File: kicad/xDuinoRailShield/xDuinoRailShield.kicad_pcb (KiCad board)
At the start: 2 copper layers, 36 parts, among them J5 Screw_Terminal_01x02, Q2 S8050, Q3 S8550, Q4 S8050, Q5 S8550, U1 TPS5430DDA, U2 6N137, U3 EL817

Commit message: Heavy refactoring
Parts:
- removed D2: D, Diode_SMD:D_SMA
- added D9: SS54, Diode_SMD:D_SMA, F.Cu at (153.9, 69.5)
- D4: value D_Schottky -> SS54; footprint Diode_SMD:D_SMC -> Diode_SMD:D_SMA
- D6, D7, D8: value D -> SS54
- R7: value 22 -> 20

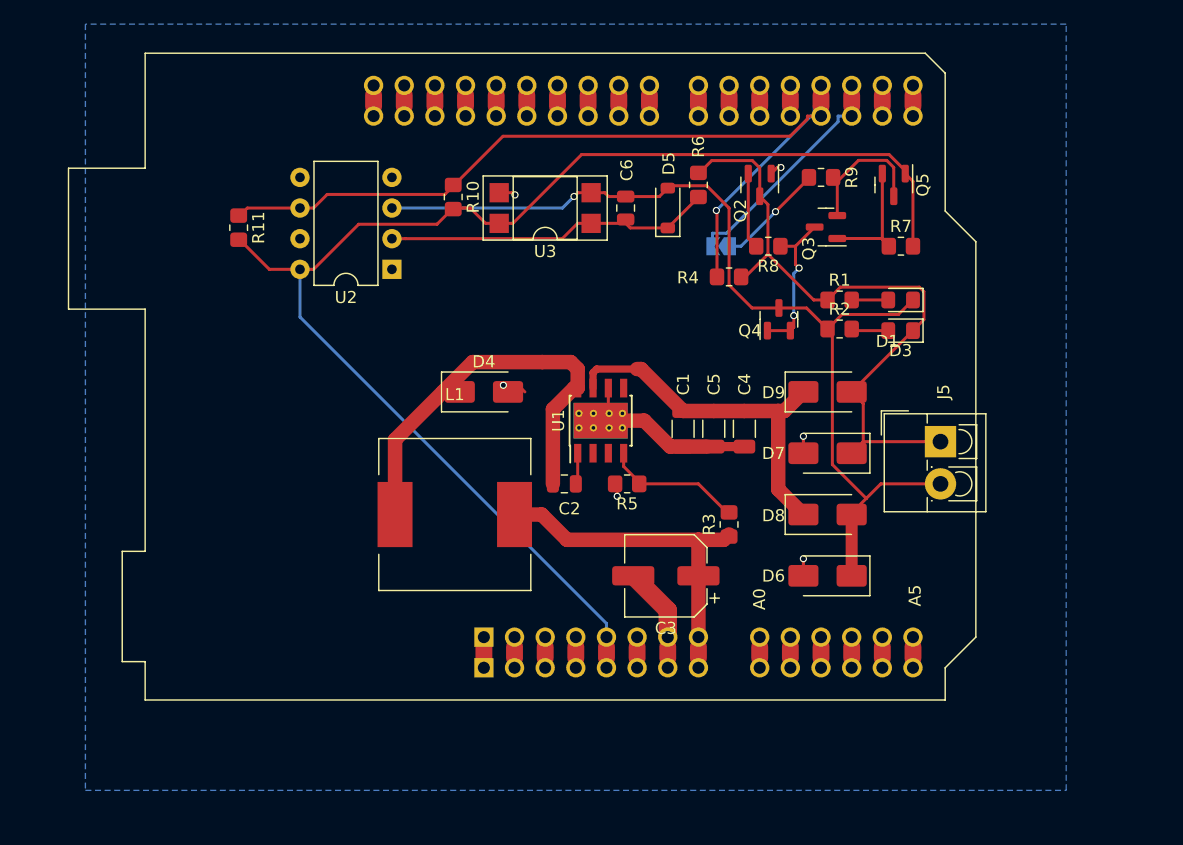
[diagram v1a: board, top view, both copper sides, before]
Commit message: More options, more Partnumbers
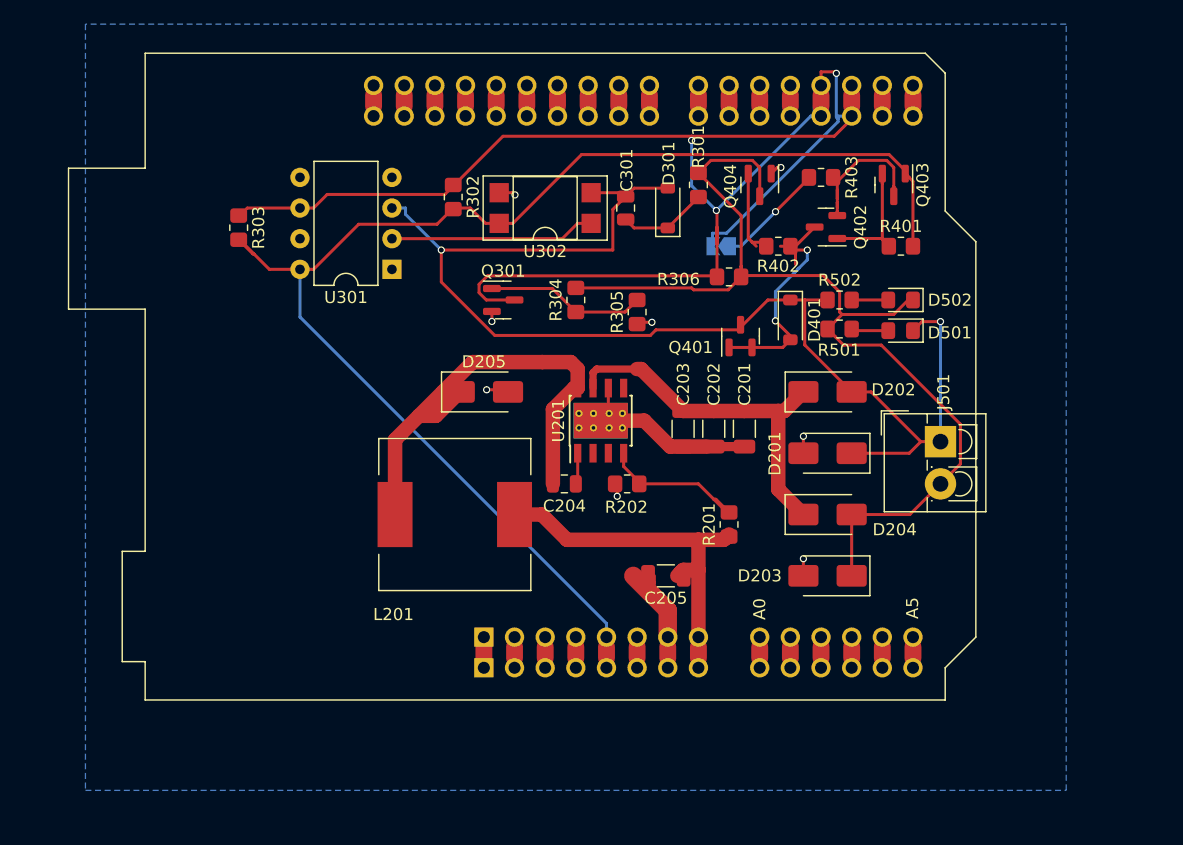
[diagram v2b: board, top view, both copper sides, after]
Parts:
- added D401: 1N4148W, Diode_SMD:D_SOD-123, F.Cu at (150.8, 63.5)
- added Q301: T2N7002BK, Package_TO_SOT_SMD:SOT-23, F.Cu at (127.0, 61.9)
- added R304: 6k8, Resistor_SMD:R_0805_2012Metric_Pad1.20x1.40mm_HandSolder, F.Cu at (133.0, 61.9)
- added R305: 6k8, Resistor_SMD:R_0805_2012Metric_Pad1.20x1.40mm_HandSolder, F.Cu at (138.1, 62.9)
- C205: renamed from C3; footprint Capacitor_SMD:CP_Elec_6.3x3.9 -> Capacitor_SMD:C_1206_3216Metric
- moved Q401 3.47 mm to (146.7, 64.9)
- moved R402 0.83 mm to (149.8, 57.4)
- renumbered A1 to A501, C4 to C201, C5 to C202, C1 to C203, C2 to C204, C6 to C301, D7 to D201, D9 to D202, D6 to D203, D8 to D204, D4 to D205, D5 to D301, D3 to D501, D1 to D502, J5 to J501, JP_RAILCOM1 to JP_RAILCOM401, L1 to L201, Q4 to Q401, Q3 to Q402, Q5 to Q403, Q2 to Q404, R3 to R201, R5 to R202, R6 to R301, R10 to R302, R11 to R303, R4 to R306, R7 to R401, R8 to R402, R9 to R403, R2 to R501, R1 to R502, U1 to U201, U2 to U301, U3 to U302
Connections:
- net Net-(D8-K) renamed DCC_VIN
- A501 pad 17: RAILCOM_DATA -> DCC_MM
- A501 pad 18: DCC_MM -> RAILCOM_DATA
- C301 pad 1: Net-(D5-K) -> Net-(D301-K)
- C301 pad 2: DCC_1 -> /DCC1
- D201 pad 1: DCC_0 -> /DCC1
- D202 pad 2: DCC_0 -> /DCC1
- D203 pad 1: DCC_1 -> /DCC0
- D204 pad 2: DCC_1 -> /DCC0
- D301 pad 1: Net-(D5-K) -> Net-(D301-K)
- D301 pad 2: DCC_1 -> /DCC1
- D501 pad 1: DCC_0 -> /DCC1
- D502 pad 1: DCC_1 -> /DCC0
- J501 pad 1: DCC_0 -> /DCC1
- J501 pad 2: DCC_1 -> /DCC0
- Q401 pad 3: DCC_1 -> /DCC1
- Q404 pad 3: DCC_0 -> /DCC0
- R301 pad 1: DCC_0 -> /DCC0
- R301 pad 2: Net-(D5-K) -> Net-(D301-K)
- R306 pad 1: DCC_0 -> /DCC0
- R501 pad 1: DCC_1 -> /DCC0
- R502 pad 1: DCC_0 -> /DCC1
- U301 pad 2: Net-(D5-K) -> DCC_0_1K3
- U301 pad 3: DCC_1 -> /DCC1
- U302 pad 1: Net-(D5-K) -> DCC_0_1K3
- U302 pad 2: DCC_1 -> /DCC1
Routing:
- net /DCC1: track 0.00 -> 106.7 mm, vias 0 -> 2
- net /DCC0: track 0.00 -> 87.5 mm
- net DCC_1: track 82.8 -> 0.00 mm, vias 1 -> 0
- net DCC_0: track 54.4 -> 0.00 mm
- net DCC_MM: track 72.1 -> 109.8 mm, vias 1 -> 2
- net Net-(D5-K): track 27.6 -> 0.00 mm
- net DCC_0_1K3: track 0.00 -> 17.0 mm
- net Net-(Q301-G): track 0.00 -> 13.3 mm
- net RAILCOM_DATA: track 19.4 -> 28.8 mm, vias 0 -> 1
- net Net-(D401-A): track 12.8 -> 20.7 mm
- net Net-(D301-K): track 0.00 -> 7.41 mm
- net GND: track 32.0 -> 36.9 mm, vias 6 -> 8
- net Net-(D205-K): track 34.8 -> 39.0 mm
- net VCC: track 29.4 -> 32.0 mm
- net +5V: track 111.9 -> 114.2 mm
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
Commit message: Leiterbahnbreiten anpassen
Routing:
- net GND: track 36.9 -> 63.5 mm, vias 8 -> 13
- net DCC_MM: track 109.8 -> 118.0 mm
- net RAILCOM_DATA: track 28.8 -> 21.5 mm, vias 1 -> 0
- net /DCC0: track 87.5 -> 84.9 mm
- net +5V: track 114.2 -> 116.6 mm
- net /DCC1: track 106.7 -> 105.4 mm, vias 2 -> 1
- net Net-(Q402-E): track 10.8 -> 9.97 mm

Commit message: Edge cuts
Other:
- board outline added: 68.6 x 53.3 mm
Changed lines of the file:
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@@
       ))
   )
+  (gr_line (start 163.503242 43.117028) (end 161.96181 41.575596)
+    (stroke (width 0.15) (type default)) (layer "Edge.Cuts"))
+  (gr_line (start 166.04 89.84) (end 166.04 56.82)
+    (stroke (width 0.15) (type default)) (layer "Edge.Cuts"))
+  (gr_line (start 161.96181 41.575596) (end 97.46 41.58)
+    (stroke (width 0.15) (type default)) (layer "Edge.Cuts"))
+  (gr_line (start 163.5 92.38) (end 166.04 89.84)
+    (stroke (width 0.15) (type default)) (layer "Edge.Cuts"))
+  (gr_line (start 163.5 54.28) (end 163.503242 43.117028)
+    (stroke (width 0.15) (type default)) (layer "Edge.Cuts"))
+  (gr_line (start 97.46 41.58) (end 97.46 94.92)
+    (stroke (width 0.15) (type default)) (layer "Edge.Cuts"))
+  (gr_line (start 163.5 94.92) (end 163.5 92.38)
+    (stroke (width 0.15) (type default)) (layer "Edge.Cuts"))
+  (gr_line (start 166.04 56.82) (end 163.5 54.28)
+    (stroke (width 0.15) (type default)) (layer "Edge.Cuts"))
+  (gr_line (start 97.46 94.92) (end 163.5 94.92)
+    (stroke (width 0.15) (type default)) (layer "Edge.Cuts"))
   (gr_text "ICSP" (at 161.492899 64.565 -90) (layer "Dwgs.User")
     (effects (font (size 1 1) (thickness 0.15)))
@@
     (polygon
       (pts
-        (xy 87.3 39.04)
-        (xy 87.3 102.54)
-        (xy 173.66 102.54)
+        (xy 89.84 39.04)
+        (xy 89.84 97.46)
+        (xy 173.66 97.46)
         (xy 173.66 39.04)
       )

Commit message: Another iteration on the layout
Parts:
- J501: footprint TerminalBlock_4Ucon:TerminalBlock_4Ucon_1x02_P3.50mm_Vertical -> TerminalBlock:TerminalBlock_bornier-2_P5.08mm
- U302: footprint Package_DIP:DIP-4_W7.62mm_SMDSocket_SmallPads -> Package_DIP:DIP-4_W8.89mm_SMDSocket_LongPads
- moved C301 2.98 mm to (139.7, 52.7), turned to 180 degrees
- moved C205 2.61 mm to (138.1, 83.7), turned to -90 degrees
- moved D301 2.54 mm to (140.6, 56.8)
- moved R201 2.54 mm to (143.2, 80.5)
- moved Q301 2.21 mm to (128.5, 60.3), turned to 180 degrees
- moved R302 1.38 mm to (121.8, 52.4)
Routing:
- net VCC: track 32.0 -> 26.7 mm
- net DCC_MM: track 118.0 -> 113.1 mm
- net Net-(U201-VSENSE): track 13.4 -> 9.06 mm
- net Net-(Q301-G): track 13.3 -> 9.72 mm
- net Net-(D401-A): track 20.7 -> 18.0 mm
- net unconnected-(A501-SDA/A4-Pad31): track 2.54 -> 0.00 mm
- net unconnected-(A501-SCL/A5-Pad32)_0: track 2.54 -> 0.00 mm
- net unconnected-(A501-D9-Pad24)_0: track 2.54 -> 0.00 mm
- net unconnected-(A501-D8-Pad23)_0: track 2.54 -> 0.00 mm
- net unconnected-(A501-D7-Pad22): track 2.54 -> 0.00 mm
- net unconnected-(A501-D6-Pad21)_0: track 2.54 -> 0.00 mm
- net unconnected-(A501-D5-Pad20): track 2.54 -> 0.00 mm
- net unconnected-(A501-D4-Pad19): track 2.54 -> 0.00 mm
- net unconnected-(A501-D1/TX-Pad16): track 2.54 -> 0.00 mm
- net unconnected-(A501-D13-Pad28): track 2.54 -> 0.00 mm
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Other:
- board size 68.6 x 53.3 mm -> 63.5 x 53.3 mm

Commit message: xXiaoCentralMini
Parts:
- removed A501: Arduino_UNO_R3, Olis_Footprints:Arduino_UNO_R3_Double_Rows
- removed C201, C202, C203, C205: 10uF, Capacitor_SMD:C_1206_3216Metric
- removed C204: 10nF, Capacitor_SMD:C_0805_2012Metric
- removed C301: 1nF, Capacitor_SMD:C_0805_2012Metric
- removed D201, D202, D203, D204, D205: SS54, Diode_SMD:D_SMA
- removed D301, D401: 1N4148W, Diode_SMD:D_SOD-123
- removed D501, D502: LED, LED_SMD:LED_0805_2012Metric_Pad1.15x1.40mm_HandSolder
- removed J501: Screw_Terminal_01x02, TerminalBlock:TerminalBlock_bornier-2_P5.08mm
- removed JP_RAILCOM401: SolderJumper_2_Open, Jumper:SolderJumper-2_P1.3mm_Open_TrianglePad1.0x1.5mm
- removed L201: 22uH, Inductor_SMD:L_12x12mm_H8mm
- removed Q301: T2N7002BK, Package_TO_SOT_SMD:SOT-23
- removed Q401, Q404: S8050, Package_TO_SOT_SMD:SOT-23
- removed Q402, Q403: S8550, Package_TO_SOT_SMD:SOT-23
- removed R201, R403: 10k, Resistor_SMD:R_0805_2012Metric_Pad1.20x1.40mm_HandSolder
- removed R202: 1.58k, Resistor_SMD:R_0805_2012Metric_Pad1.20x1.40mm_HandSolder
- removed R301: 1k3, Resistor_SMD:R_0805_2012Metric_Pad1.20x1.40mm_HandSolder
- removed R302: 220R, Resistor_SMD:R_0805_2012Metric_Pad1.20x1.40mm_HandSolder
- removed R303: 5k, Resistor_SMD:R_0805_2012Metric_Pad1.20x1.40mm_HandSolder
- removed R304, R305, R402: 6k8, Resistor_SMD:R_0805_2012Metric_Pad1.20x1.40mm_HandSolder
- removed R306: 22k, Resistor_SMD:R_0805_2012Metric_Pad1.20x1.40mm_HandSolder
- removed R401: 20, Resistor_SMD:R_0805_2012Metric_Pad1.20x1.40mm_HandSolder
- removed R501, R502: 3k3, Resistor_SMD:R_0805_2012Metric_Pad1.20x1.40mm_HandSolder
- removed U201: TPS5430DDA, Package_SO:TI_SO-PowerPAD-8_ThermalVias
- removed U301: 6N137, Package_DIP:DIP-8_W7.62mm
- removed U302: EL817, Package_DIP:DIP-4_W8.89mm_SMDSocket_LongPads
- added A1: Arduino_UNO_R3, Module:Arduino_UNO_R3, B.Cu at (125.4, 92.4)
- added D1: SS54, Diode_SMD:D_SMA, F.Cu at (153.9, 72.1)
- added D2: SS54, Diode_SMD:D_SMA, F.Cu at (153.9, 76.6)
- added D3: SS54, Diode_SMD:D_SMA, F.Cu at (153.9, 81.2)
- added D4: SS54, Diode_SMD:D_SMA, F.Cu at (153.9, 85.7)
- added J1: Screw_Terminal_01x02, TerminalBlock:TerminalBlock_bornier-2_P5.08mm, F.Cu at (163.5, 84.8)
- added J2: AudioJack2_Ground, Connector_Audio:Jack_3.5mm_CUI_SJ-3523-SMT_Horizontal, F.Cu at (159.9, 63.1)
- added J3: PLUXX22, Connector_PinHeader_1.27mm:PinHeader_2x11_P1.27mm_Vertical_SMD, B.Cu at (120.9, 81.0)
- added J4: 21mtc, Connector_PinSocket_1.27mm:PinSocket_2x11_P1.27mm_Vertical_SMD, F.Cu at (121.1, 81.0)
- added JP1: DAC_OUTPUT_SELECT, Jumper:SolderJumper-3_P1.3mm_Bridged12_RoundedPad1.0x1.5mm, B.Cu at (149.5, 59.4)
- added Q2: S8050, Package_TO_SOT_SMD:SOT-23, F.Cu at (138.5, 62.8)
- added Q3: S8550, Package_TO_SOT_SMD:SOT-23, F.Cu at (136.2, 66.7)
- added Q4: S8550, Package_TO_SOT_SMD:SOT-23, F.Cu at (132.0, 61.0)
- added Q5: S8050, Package_TO_SOT_SMD:SOT-23, F.Cu at (136.5, 58.4)
- added R10: 6k8, Resistor_SMD:R_0603_1608Metric_Pad0.98x0.95mm_HandSolder, F.Cu at (135.6, 62.8)
- added R11: 10k, Resistor_SMD:R_0603_1608Metric_Pad0.98x0.95mm_HandSolder, F.Cu at (133.0, 56.8)
- added R8: 22k, Resistor_SMD:R_0603_1608Metric_Pad0.98x0.95mm_HandSolder, F.Cu at (144.8, 56.8)
- added R9: 20, Resistor_SMD:R_0603_1608Metric_Pad0.98x0.95mm_HandSolder, F.Cu at (132.1, 64.4)
- added RV1: 10K, Potentiometer_SMD:Potentiometer_ACP_CA6-VSMD_Vertical, F.Cu at (155.9, 51.7)
- added U1: L78L05_SOT89, Package_TO_SOT_SMD:SOT-89-3, F.Cu at (145.4, 79.4)
- added U7: MOUDLE-SEEEDUINO-XIAO-ESP32C3, xiao ESP32C3_PCB:MOUDLE14P-SMD-2.54-21X17.8MM, F.Cu at (123.8, 68.3)
- added U8: DRV8872DDA, Package_SO:Texas_HTSOP-8-1EP_3.9x4.9mm_P1.27mm_EP2.95x4.9mm_Mask2.4x3.1mm_ThermalVias, F.Cu at (134.9, 75.8)
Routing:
- net DCC_MM: track 113.1 -> 18.0 mm, vias 2 -> 0
- net +5V: track 117.9 -> 39.2 mm
- net GND: track 65.2 -> 14.6 mm, vias 13 -> 8
- net /Loco Adapters/MOTOR+: track 0.00 -> 46.4 mm, vias 0 -> 2
- net Net-(D205-K): track 39.0 -> 0.00 mm
- net /DCC1: track 106.5 -> 70.8 mm, vias 1 -> 2
- net /MCU Carrier Board/DAC_NUCLEO: track 0.00 -> 34.1 mm
- net /MCU Carrier Board/DAC_ADAFRUIT_SPARKFUN: track 0.00 -> 33.0 mm
- net /Loco Adapters/SPEAKER0: track 0.00 -> 29.4 mm, vias 0 -> 1
- net VCC: track 26.7 -> 0.00 mm
- net /Loco Adapters/MOTOR-: track 0.00 -> 25.5 mm, vias 0 -> 1
- net Net-(D401-A): track 18.0 -> 0.00 mm, vias 2 -> 0
- net DCC_0_1K3: track 17.0 -> 0.00 mm
- net DCC_VIN: track 30.4 -> 13.5 mm
- net /Loco Adapters/+5V: track 0.00 -> 16.3 mm
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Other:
- board size 63.5 x 53.3 mm -> 63.6 x 53.4 mm

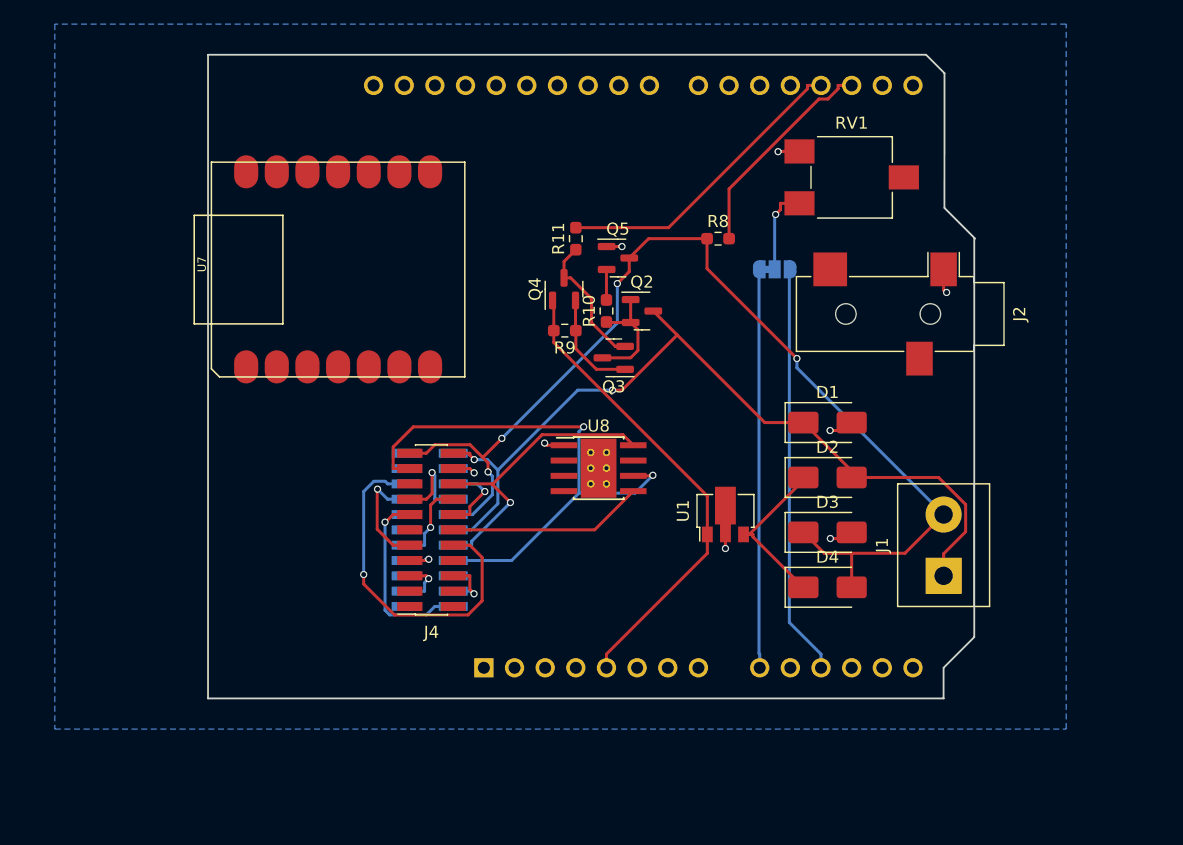
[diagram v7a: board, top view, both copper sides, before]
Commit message: Draft of loco decoder
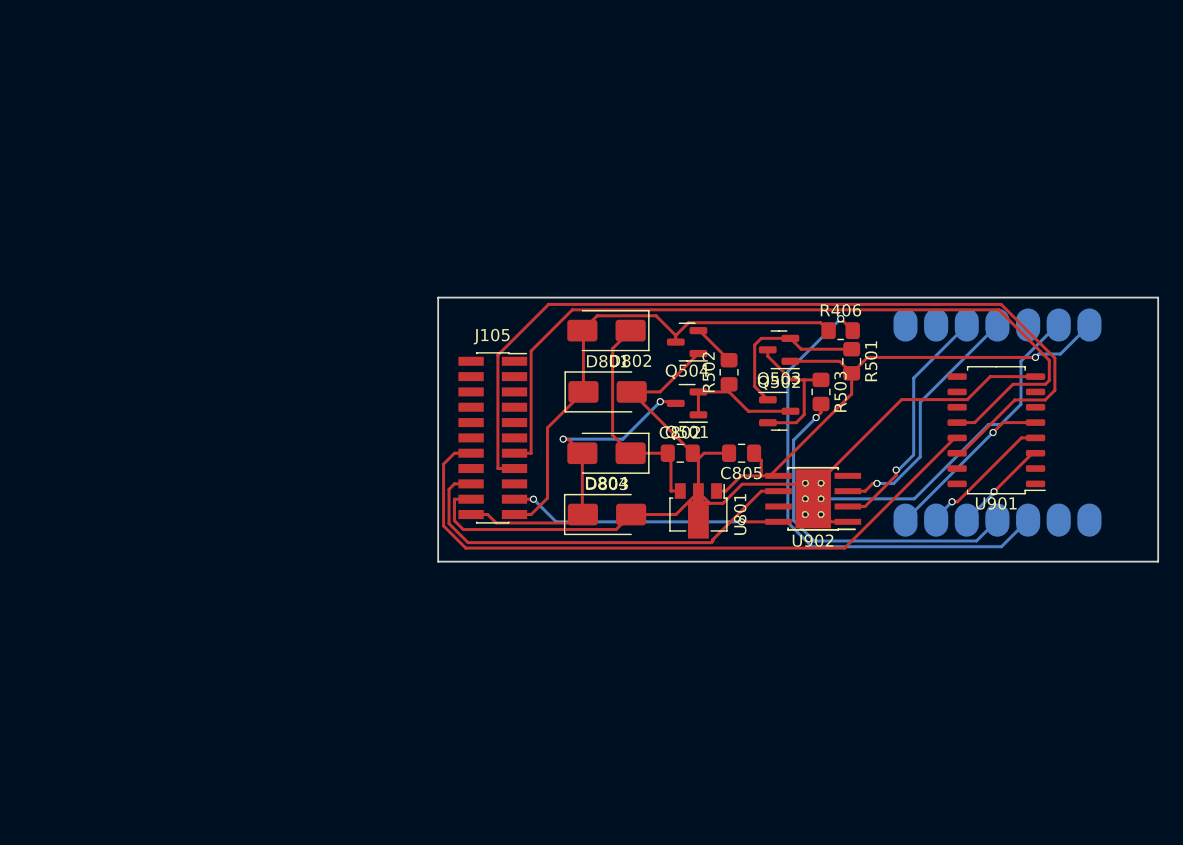
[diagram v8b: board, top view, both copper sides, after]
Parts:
- removed A1: Arduino_UNO_R3, Module:Arduino_UNO_R3
- removed D1, D2, D3, D4: SS54, Diode_SMD:D_SMA
- removed J1: Screw_Terminal_01x02, TerminalBlock:TerminalBlock_bornier-2_P5.08mm
- removed J2: AudioJack2_Ground, Connector_Audio:Jack_3.5mm_CUI_SJ-3523-SMT_Horizontal
- removed J3: PLUXX22, Connector_PinHeader_1.27mm:PinHeader_2x11_P1.27mm_Vertical_SMD
- removed J4: 21mtc, Connector_PinSocket_1.27mm:PinSocket_2x11_P1.27mm_Vertical_SMD
- removed JP1: DAC_OUTPUT_SELECT, Jumper:SolderJumper-3_P1.3mm_Bridged12_RoundedPad1.0x1.5mm
- removed Q2, Q5: S8050, Package_TO_SOT_SMD:SOT-23
- removed Q3, Q4: S8550, Package_TO_SOT_SMD:SOT-23
- removed R10: 6k8, Resistor_SMD:R_0603_1608Metric_Pad0.98x0.95mm_HandSolder
- removed R11: 10k, Resistor_SMD:R_0603_1608Metric_Pad0.98x0.95mm_HandSolder
- removed R8: 22k, Resistor_SMD:R_0603_1608Metric_Pad0.98x0.95mm_HandSolder
- removed R9: 20, Resistor_SMD:R_0603_1608Metric_Pad0.98x0.95mm_HandSolder
- removed RV1: 10K, Potentiometer_SMD:Potentiometer_ACP_CA6-VSMD_Vertical
- removed U1: L78L05_SOT89, Package_TO_SOT_SMD:SOT-89-3
- removed U7: MOUDLE-SEEEDUINO-XIAO-ESP32C3, xiao ESP32C3_PCB:MOUDLE14P-SMD-2.54-21X17.8MM
- removed U8: DRV8872DDA, Package_SO:Texas_HTSOP-8-1EP_3.9x4.9mm_P1.27mm_EP2.95x4.9mm_Mask2.4x3.1mm_ThermalVias
- added C802: 1uF, Capacitor_SMD:C_0805_2012Metric_Pad1.18x1.45mm_HandSolder, F.Cu at (141.7, 74.6)
- added C805: 47uF, Capacitor_SMD:C_0805_2012Metric_Pad1.18x1.45mm_HandSolder, F.Cu at (146.8, 74.6)
- added D801: SS34, Diode_SMD:D_SMA, F.Cu at (135.7, 69.5)
- added D802: SS34, Diode_SMD:D_SMA, F.Cu at (135.6, 64.4)
- added D803: SS34, Diode_SMD:D_SMA, F.Cu at (135.6, 79.7)
- added D804: SS34, Diode_SMD:D_SMA, F.Cu at (135.6, 74.6)
- added J105: 21mtc_mrkl, Connector_PinSocket_1.27mm:PinSocket_2x11_P1.27mm_Vertical_SMD, F.Cu at (126.1, 73.3)
- added Q501: S8050, Package_TO_SOT_SMD:SOT-23, F.Cu at (142.2, 70.5)
- added Q502: S8550, Package_TO_SOT_SMD:SOT-23, F.Cu at (149.9, 71.1)
- added Q503: S8550, Package_TO_SOT_SMD:SOT-23, F.Cu at (149.9, 66.0)
- added Q504: S8050, Package_TO_SOT_SMD:SOT-23, F.Cu at (142.2, 65.4)
- added R406: 22k, Resistor_SMD:R_0805_2012Metric_Pad1.20x1.40mm_HandSolder, F.Cu at (155.0, 64.4)
- added R501: 20, Resistor_SMD:R_0805_2012Metric_Pad1.20x1.40mm_HandSolder, F.Cu at (155.9, 67.0)
- added R502: 6k8, Resistor_SMD:R_0805_2012Metric_Pad1.20x1.40mm_HandSolder, F.Cu at (145.7, 67.9)
- added R503: 10k, Resistor_SMD:R_0805_2012Metric_Pad1.20x1.40mm_HandSolder, F.Cu at (153.3, 69.5)
- added U601: MOUDLE-SEEEDUINO-XIAO-ESP32C3, xiao ESP32C3_PCB:MOUDLE14P-SMD-2.54-21X17.8MM, B.Cu at (157.5, 81.0)
- added U801: L78L05_SOT89, Package_TO_SOT_SMD:SOT-89-3, F.Cu at (143.2, 79.7)
- added U901: ULN2003A, Package_SO:SOIC-16_4.55x10.3mm_P1.27mm, F.Cu at (167.9, 72.7)
- added U902: DRV8872DDA, Package_SO:Texas_HTSOP-8-1EP_3.9x4.9mm_P1.27mm_EP2.95x4.9mm_Mask2.4x3.1mm_ThermalVias, F.Cu at (152.7, 78.4)
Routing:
- net GND: track 14.6 -> 114.0 mm, vias 8 -> 0
- net AMP_AUX1: track 0.00 -> 73.5 mm
- net AMP_AUX3: track 0.00 -> 66.7 mm
- net AMP_AUX2: track 0.00 -> 54.9 mm
- net /DCC0: track 90.3 -> 41.3 mm, vias 4 -> 0
- net /Loco Adapters/MOTOR+: track 46.4 -> 0.00 mm, vias 2 -> 0
- net /DCC1: track 70.8 -> 27.7 mm
- net /Connectors 21mtc / PluXX / NEMA/AMP_MOTOR0: track 0.00 -> 34.7 mm
- net /MCU Carrier Board/DAC_NUCLEO: track 34.1 -> 0.00 mm
- net /MCU Carrier Board/DAC_ADAFRUIT_SPARKFUN: track 33.0 -> 0.00 mm
- net /Loco Adapters/SPEAKER0: track 29.4 -> 0.00 mm, vias 1 -> 0
- net /Loco Adapters/MOTOR-: track 25.5 -> 0.00 mm, vias 1 -> 0
- net DCC_MM: track 18.0 -> 41.8 mm, vias 0 -> 1
- net /Connectors 21mtc / PluXX / NEMA/AMP_MOTOR1: track 0.00 -> 22.7 mm, vias 0 -> 2
- net /MCU Carrier Board/MOTOR0: track 0.00 -> 20.8 mm, vias 0 -> 1
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- removed copper zone on B.Cu, net GND
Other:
- board size 63.6 x 53.4 mm -> 59.7 x 21.9 mm
- board text removed: "ICSP"
